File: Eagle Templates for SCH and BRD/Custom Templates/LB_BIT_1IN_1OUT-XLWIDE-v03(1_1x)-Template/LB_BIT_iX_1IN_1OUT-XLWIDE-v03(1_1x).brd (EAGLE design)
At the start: 44.4 x 38 mm, 17 parts, among them U1 LV321SOT23-5, U2 LV321SOT23-5

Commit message: added bitlab logo and made minor changes to board templates. Updated littlebits library.
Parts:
- removed FRAME1: FRAME-LETTER, LITTLEBITS:FABDWG01-OHW
- added U$4: (no value), LITTLEBITS:BITLAB-LOGO
- added U$5: FRAME-LETTER, LITTLEBITS:FABDWG01-OHW
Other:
- board text added: "iX Name Here"
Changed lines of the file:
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@@
 <setting verticaltext="up"/>
 </settings>
-<grid distance="0.1" unitdist="mm" unit="mm" style="lines" multiple="1" display="yes" altdistance="0.01" altunitdist="mm" altunit="mm"/>
+<grid distance="0.05" unitdist="mm" unit="mm" style="lines" multiple="1" display="yes" altdistance="0.01" altunitdist="mm" altunit="mm"/>
 <layers>
 <layer number="1" name="Top" color="4" fill="1" visible="yes" active="yes"/>
@@
 <layer number="113" name="extra" color="10" fill="1" visible="yes" active="yes"/>
 <layer number="116" name="Patch_BOT" color="9" fill="4" visible="yes" active="yes"/>
+<layer number="118" name="Rect_Pads" color="7" fill="1" visible="no" active="yes"/>
 <layer number="121" name="_tsilk" color="7" fill="1" visible="yes" active="yes"/>
 <layer number="122" name="_bsilk" color="7" fill="1" visible="yes" active="yes"/>
@@
 <dimension x1="0.11" y1="9.475" x2="26.31" y2="9.475" x3="13.21" y3="-4.945" textsize="1.778" layer="113"/>
 <text x="24.3" y="6.1" size="0.8128" layer="16" font="vector" ratio="12" rot="MR90">revX</text>
+<text x="23.9" y="22.91" size="1.3" layer="21" font="vector" rot="SR270" align="center">iX Name Here</text>
 </plain>
 <attributes>
@@
 <attribute name="VOLTAGE" value="" x="-4.6" y="23.4" size="1.778" layer="28" rot="MR90" display="off"/>
 </element>
-<element name="FRAME1" library="LITTLEBITS" package="FABDWG01-OHW" value="FRAME-LETTER" x="0" y="0"/>
 <element name="U$3" library="ohw-logo" package="OSHW_FILLX150_NOTEXT" value="" x="21.7" y="36.4" rot="MR90"/>
+<element name="U$5" library="LITTLEBITS" package="FABDWG01-OHW" value="FRAME-LETTER" x="0.003" y="-0.0075"/>
+<element name="U$4" library="LITTLEBITS" package="BITLAB-LOGO" value="" x="22.65" y="27.2" rot="R270"/>
 </elements>
 <signals>

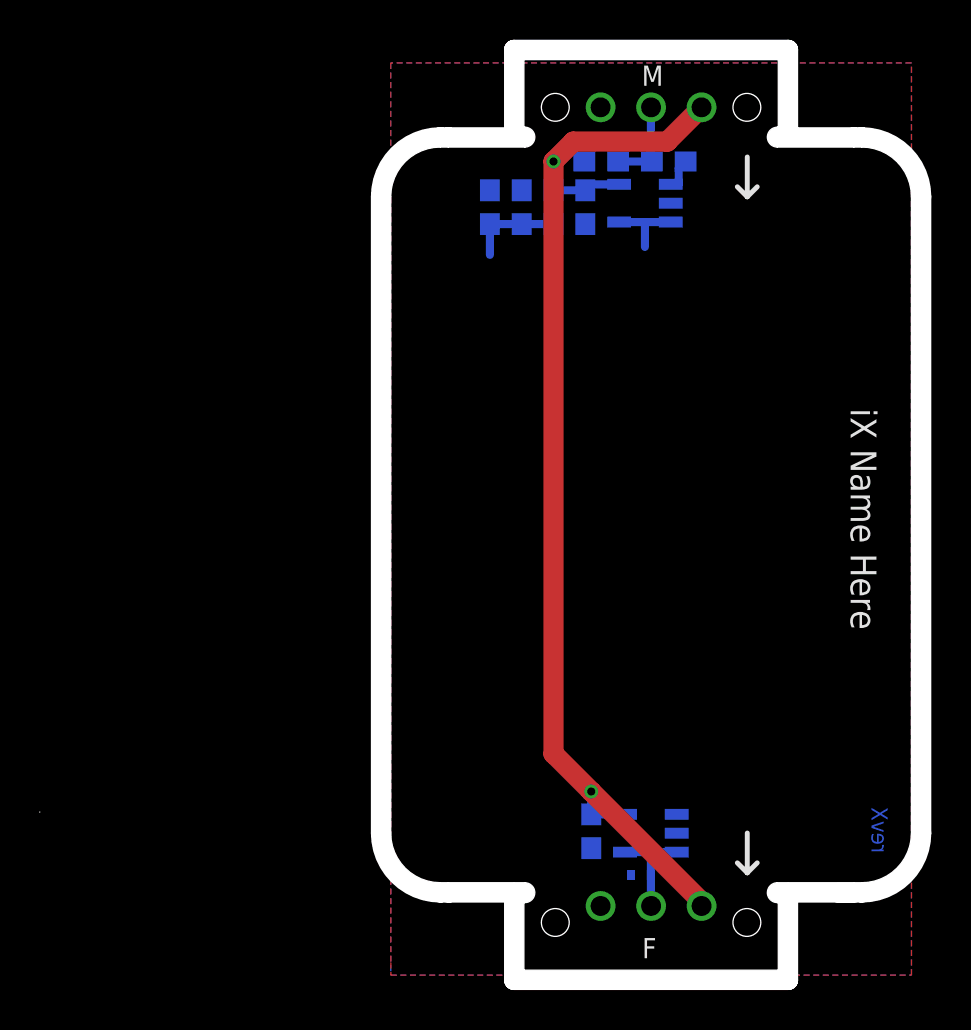
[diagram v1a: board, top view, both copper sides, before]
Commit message: Updated templates
- Added ferrite beads
- Moved text and annotations off of Nets layer
- Minor layout changes
- Removed I/O/W prefix from reference designators
- Removed output stage components from output bits
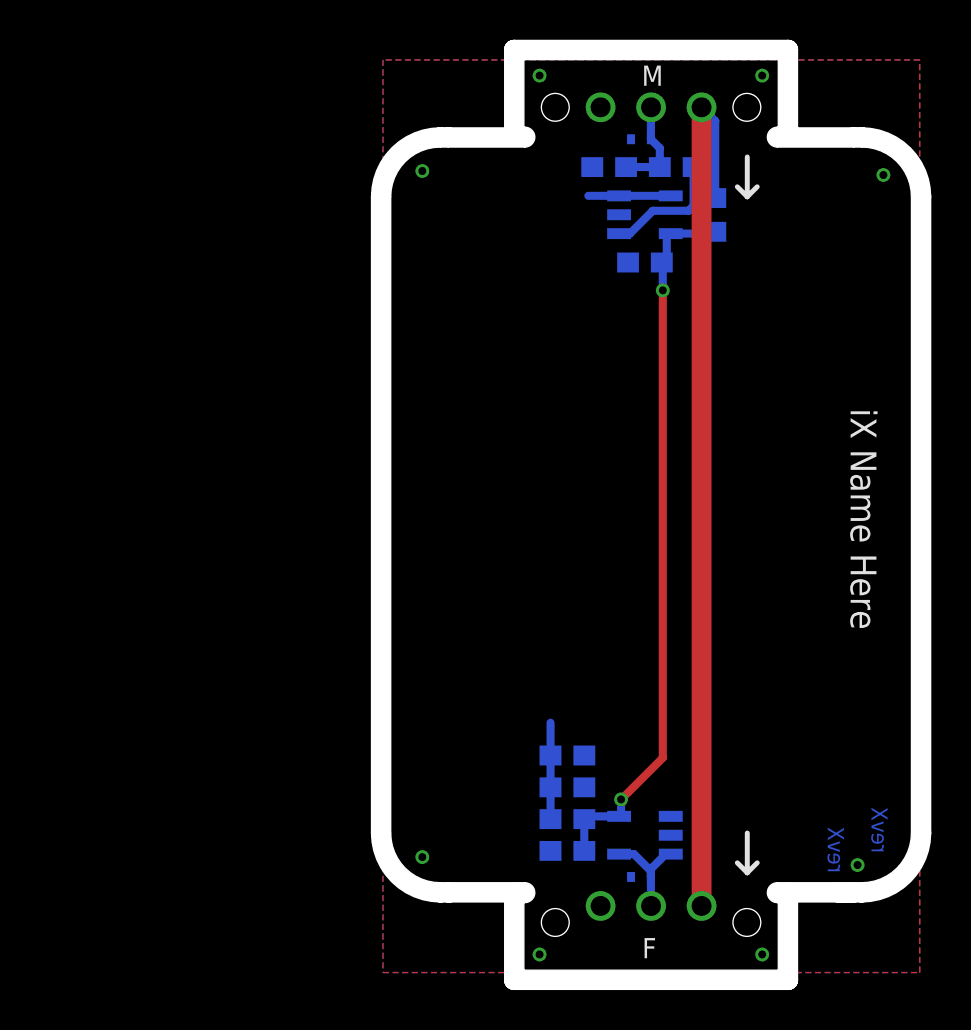
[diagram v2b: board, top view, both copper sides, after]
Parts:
- removed I?C1: 0.1uF, LITTLEBITS:CAP-0603
- removed I?C2: 10uF, LITTLEBITS:CAP-0603
- removed I?C3: 1.0uF, LITTLEBITS:CAP-0603
- removed I?R1: 1meg, LITTLEBITS:RES-0603
- removed I?R2: 10K, LITTLEBITS:RES-0603
- removed I?R3, I?R4: 3K3, LITTLEBITS:RES-0603
- removed I?TVS1, I?TVS2: ESD9B5.0ST5G, LITTLEBITS:SOD-923
- added C1: 0.1uF, LITTLEBITS:CAP-0603
- added C2: 10uF, LITTLEBITS:CAP-0603
- added C3: 1.0uF, LITTLEBITS:CAP-0603
- added FB1: FERRITE-BEAD0603, LITTLEBITS:R0603
- added R1: 1meg, LITTLEBITS:RES-0603
- added R2: 10K, LITTLEBITS:RES-0603
- added R3, R4: 3K3, LITTLEBITS:RES-0603
- added TVS1, TVS2: ESD9B5.0ST5G, LITTLEBITS:SOD-923
- U$1: value OSHWCREDIT -> OSHW-LOGOL; device LITTLEBITS:OSHWCREDIT -> LITTLEBITS131206:OSHW-LOGO-L
- U$2: value OSHW-LOGOL -> OSHWCREDIT; device LITTLEBITS131206:OSHW-LOGO-L -> LITTLEBITS:OSHWCREDIT
- U$5: value FRAME-LETTER -> FRAME-LETTER-OHWOHW
- moved U$2 61.9 mm to (-92.2, -64.3)
- moved U$1 50.6 mm to (-37.5, -68.2)
- moved U1 0.58 mm to (12.9, 38.2), turned to 90 degrees
- moved U2 0.32 mm to (12.9, 7.00)
- renumbered I?BSF to BSF1, I?BSM to BSM1
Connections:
- new net LB_VCC: BSF1.VCC, BSM1.VCC1, FB1.2
- net GND: now also C1.2, C2.2, C3.1, R1.1, R4.1, TVS1.1, TVS2.1; no longer I?C1.2, I?C2.2, I?C3.1, I?R1.1, I?R4.1, I?TVS1.1, I?TVS2.1
- net N$4: now also R2.1; no longer I?R2.1
- net SIG_IN: now also R1.2, R2.2, TVS1.2; no longer I?R1.2, I?R2.2, I?TVS1.2
- net SIG_OUT: now also TVS2.2; no longer I?TVS2.2
- net VCC: now also C1.1, C3.2, FB1.1, R3.2; no longer BSF1.VCC, BSM1.VCC1, I?C1.1, I?C3.2, I?R3.2
- net VREF: now also C2.1, R3.1, R4.2; no longer I?C2.1, I?R3.1, I?R4.2
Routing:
- net LB_VCC: track 0.00 -> 45.0 mm
- net VCC: track 57.0 -> 36.9 mm
- net N$4: track 1.69 -> 6.28 mm
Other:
- board size 44.4 x 38 mm -> 27.2 x 38 mm
